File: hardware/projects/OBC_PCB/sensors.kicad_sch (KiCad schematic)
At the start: 12 parts, among them U3 BMA400, U4 BMM350, U5 BMP581

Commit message: fix(hardware): apply schematic review and peripheral pin mapping
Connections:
- net GND: no longer U5.7 (INT)
- new net BARO_INT: U5.7 (INT)
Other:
- note added: "C35 at VDD (10); C36 at VDDIO (1). No traces / vias / mask under U5; keep pressure port clear. INT routed to P0.01; polling or data-ready interrupt."
- note removed: "C35 at VDD (10); C36 at VDDIO (1). No traces / vias / mask under U5; keep pressure port clear. Polling: keep INT_CONFIG.int_en = 0 (INT grounded)."

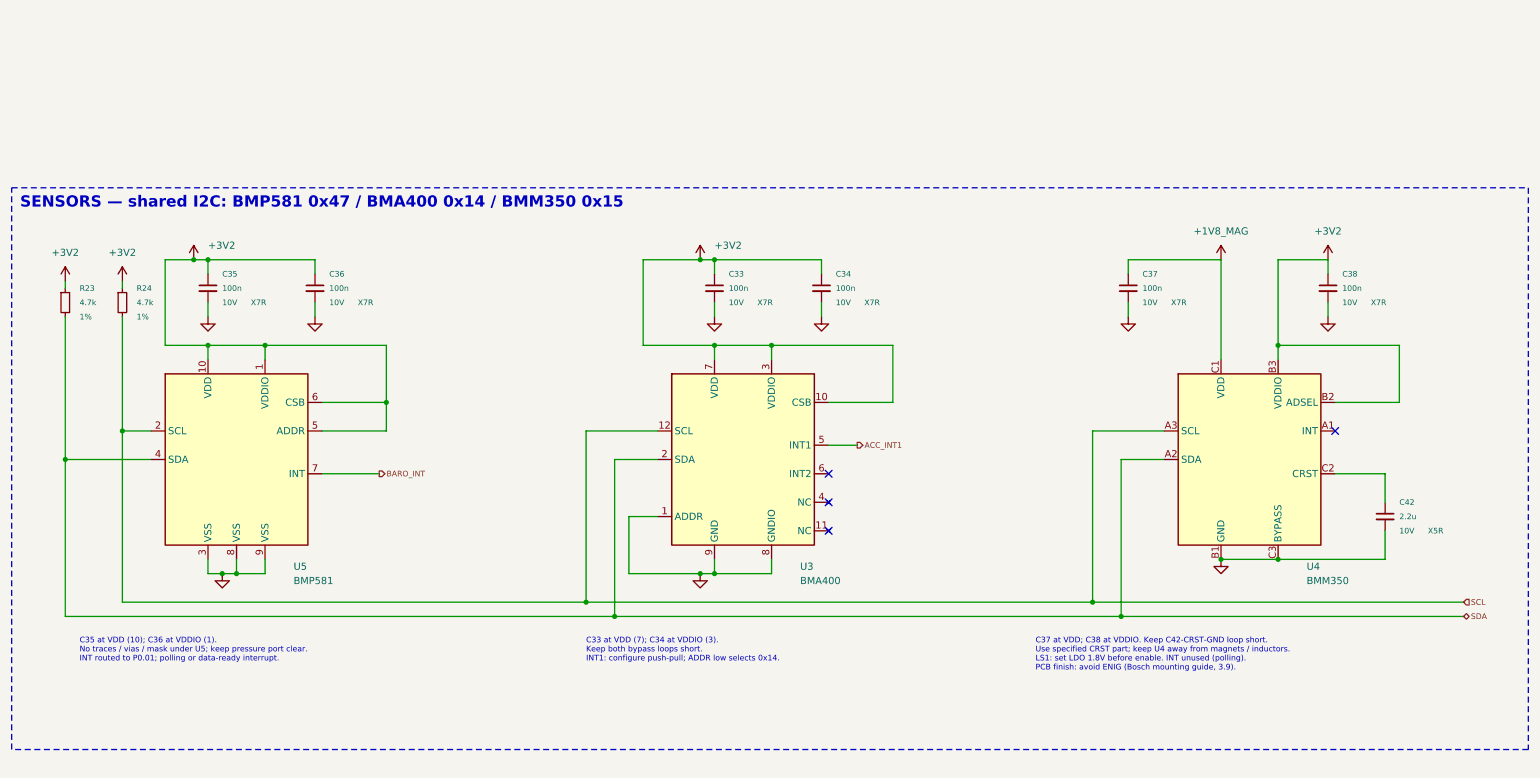
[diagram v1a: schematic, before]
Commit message: hardware: prepare QFN schematic for non-HDI boards
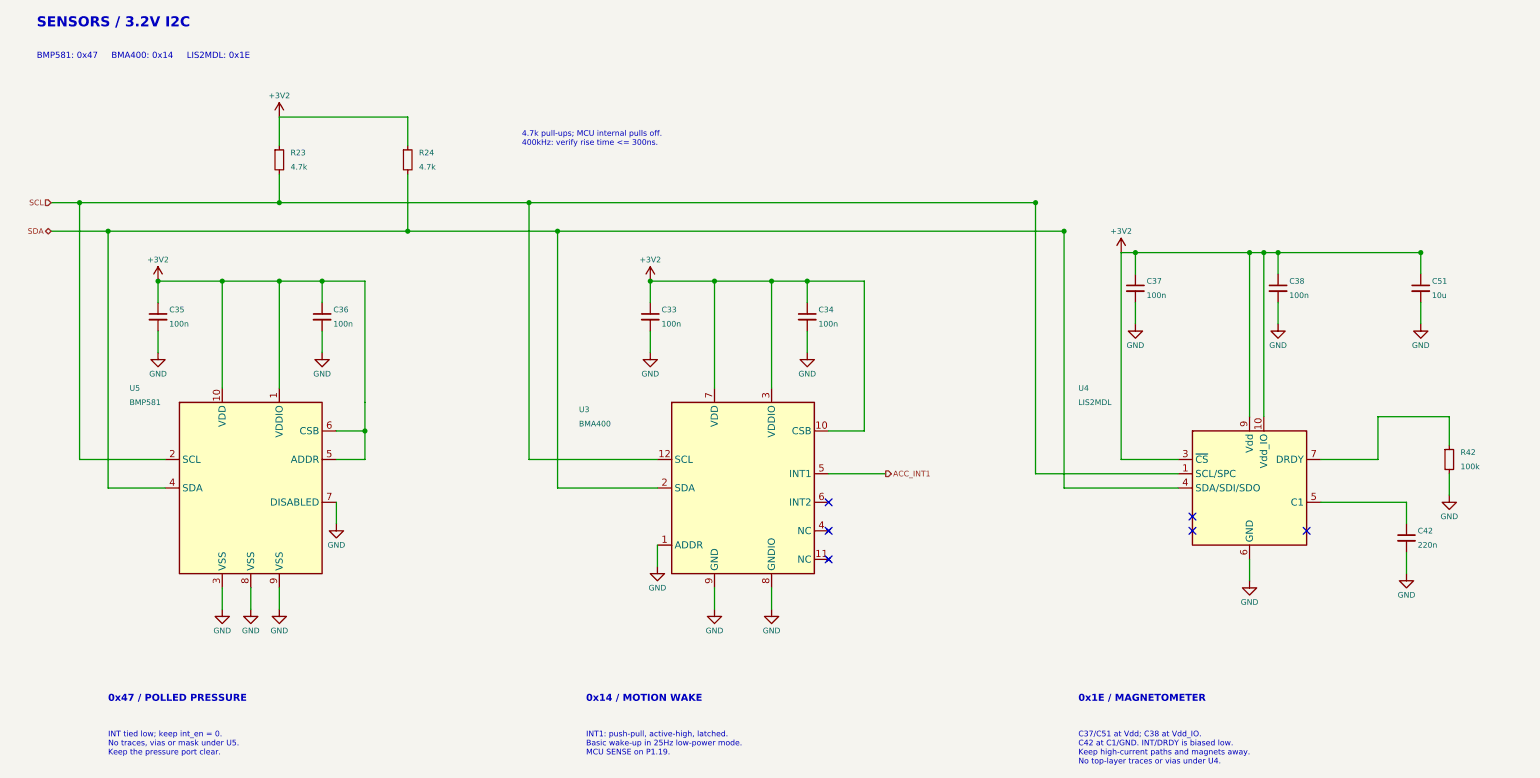
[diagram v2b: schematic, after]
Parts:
- added C51: 10u, Capacitor_SMD:C_0603_1608Metric, symbol Device:C_Small
- added R42: 100k, Resistor_SMD:R_0402_1005Metric, symbol Device:R_Small
- C42: value 2.2u -> 220n; Dielectric X5R -> X7R; ESR (none) -> < 0.2 ohm; MPN C1005X5R1A225K050BC -> (none); Manufacturer TDK -> (none); Selection basis Bosch support: BMM350 magnetometer - recommended CRST capac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 -> (none); Selection reference https://community.bosch-sensortec.com/mems-sensors-forum-jr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 -> (none)
- U4: value BMM350 -> LIS2MDL; footprint obc:BGA9_BMM350 -> Package_LGA:LGA-12_2x2mm_P0.5mm; symbol obc:BMM350 -> Sensor_Magnetic:LIS2MDL; I2C address 0x15 -> (none); Interrupt configuration Polling; INT unconnected and output disabled -> (none); MPN BMM350 -> LIS2MDLTR; Manufacturer Bosch Sensortec -> STMicroelectronics; PCB finish guidance Bosch BMM350 mounting guide section 3.9: do not use ENIG; r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 -> (none); PCB layout guide https://www.bosch-sensortec.com/media/boschsensortec/downlo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 -> (none)
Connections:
- net BARO_INT is gone; now on net GND: U5.7 (INT)
- net +3V2: now also C37.1, U4.10 (Vdd_IO), U4.3 (~{CS}), U4.9 (Vdd), C51.1; no longer U4.B2 (ADSEL), U4.B3 (VDDIO)
- net GND: now also U4.6 (GND), U4.8 (GND), C51.2, R42.2; no longer U4.B1 (GND), U4.C3 (BYPASS)
- net SCL: now also R23.2, U4.1 (SCL/SPC); no longer R24.2, U4.A3 (SCK)
- net SDA: now also R24.2, U4.4 (SDA/SDI/SDO); no longer R23.2, U4.A2 (SDA)
- net at C42.1: now also U4.5 (C1); no longer U4.C2 (CRST)
- removed net +1V8_MAG: C37.1, U4.C1 (VDD)
- new net: R42.1, U4.7 (DRDY)
- no-connect marks 4 -> 6
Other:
- note added: "0x14 / MOTION WAKE"
- note added: "0x1E / MAGNETOMETER"
- note added: "0x47 / POLLED PRESSURE"
- note added: "4.7k pull-ups; MCU internal pulls off. 400kHz: verify rise time <= 300ns."
- note added: "BMP581: 0x47 BMA400: 0x14 LIS2MDL: 0x1E"
- note added: "C37/C51 at Vdd; C38 at Vdd_IO. C42 at C1/GND. INT/DRDY is biased low. Keep high-current paths and magnets away. No top-layer traces or vias under U4."
- note added: "INT tied low; keep int_en = 0. No traces, vias or mask under U5. Keep the pressure port clear."
- note added: "INT1: push-pull, active-high, latched. Basic wake-up in 25Hz low-power mode. MCU SENSE on P1.19."
- note added: "SENSORS / 3.2V I2C"
- note removed: "C33 at VDD (7); C34 at VDDIO (3). Keep both bypass loops short. INT1: configure push-pull; ADDR low selects 0x14."
- note removed: "C35 at VDD (10); C36 at VDDIO (1). No traces / vias / mask under U5; keep pressure port clear. INT routed to P0.01; polling or data-ready interrupt."
- note removed: "C37 at VDD; C38 at VDDIO. Keep C42-CRST-GND loop short. Use specified CRST part; keep U4 away from magnets / inductors. LS1: set LDO 1.8V before enable. INT unused (polling). PCB finish: avoid ENIG (Bosch mounting guide, 3.9)."
- note removed: "SENSORS — shared I2C: BMP581 0x47 / BMA400 0x14 / BMM350 0x15"
- title: OpenBikeComputer — Sensors -> OpenBikeComputer - motion and environment
- moved on the sheet: C33, C34, C35, C36, C37, C38, C42, R23, R24, U3, U5
